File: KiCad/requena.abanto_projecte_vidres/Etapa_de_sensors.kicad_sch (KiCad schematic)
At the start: 0 parts

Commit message: avance sensores
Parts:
- added C1: 100nF, symbol Device:C
- added C2, C3: C, symbol Device:C
- added C4, C5, C6, C7, C8: 100nF, symbol Device:C_Small
- added R1, R2: R, symbol Device:R
- added U1: PN5120A0HN1, Package_DFN_QFN:HVQFN-32-1EP_5x5mm_P0.5mm_EP3.1x3.1mm, symbol RF_RFID:PN5120A0HN1
- added U2: MCP6001-OT, Package_TO_SOT_SMD:SOT-23-5, symbol Amplifier_Operational:MCP6001-OT
- added Y1: Crystal, symbol Device:Crystal
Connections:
- new net: C2.1, U1.21 (OSCIN), Y1.1
- new net: C3.1, U1.22 (OSCOUT), Y1.2
- new net: R1.2, R2.1, U2.4 (-)
- new net: C1.1, U1.16 (VMID)
- new net AN0: R2.2, U2.1
- new net GND: C1.2, C2.2, C3.2, C4.1, C5.1, C6.1, C7.1, C8.1, R1.1, U1.1 (A1), U1.10 (TVSS), U1.14 (TVSS), U1.18 (AVSS), U1.24 (ALE), U1.32 (A0), U1.33 (EP), U1.4 (DVSS), U1.5 (PVSS), U2.2 (V-)
- new net IRQ: U1.23 (IRQ)
- new net MISO: U1.17 (RX)
- new net MOSI: U1.11 (TX1)
- new net NRSTPD: U1.6 (~{NRSTPD})
- new net SCK: U1.13 (TX2)
- new net VCC: C4.2, C5.2, C6.2, C7.2, C8.2, U1.12 (TVDD), U1.15 (AVDD), U1.2 (PVDD), U1.3 (DVDD), U1.9 (SVDD), U2.5 (V+)
- new net V_SHUNT: U2.3 (+)
- no-connect marks 0 -> 7
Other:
- note added: "A INT0"
- note added: "A L'ANTENA"
- note added: "A RBXX"
- note added: "A RPXX"

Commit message: avance sensores
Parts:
- added SW1, SW3, SW4, SW5: SW_Omron_B3FS, symbol Switch:SW_Omron_B3FS
- added SW2: SW_Push_SPDT, symbol Switch:SW_Push_SPDT
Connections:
- net GND: now also SW1.1, SW3.1, SW4.1, SW5.1
- net VCC: now also SW2.2 (B)
- new net CLOSED_FC: SW2.3 (C)
- new net CLOSE_D: SW5.2
- new net DOWN_W: SW3.2
- new net OPEN_D: SW4.2
- new net OPEN_FC: SW2.1 (A)
- new net UP_W: SW1.2
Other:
- moved on the sheet: C1, C2, C3, C4, C5, C6, C7, C8, R1, R2, U1, U2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

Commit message: arreglos
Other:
- note removed: "A INT0"
- note removed: "A RPXX"
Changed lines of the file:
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@@
-		)
-	)
-	(text "A RPXX\n"
-		(exclude_from_sim no)
-		(at 94.234 148.59 0)
-		(effects
-			(font
-				(size 1.27 1.27)
-			)
 		)
 	)
@@
 		(effects
 			(font
-				(size 1.27 1.27)
-			)
-		)
-	)
-	(text "A RPXX\n"
-		(exclude_from_sim no)
-		(at 94.742 145.796 0)
-		(effects
-			(font
-				(size 1.27 1.27)
-			)
-		)
-	)
-	(text "A INT0\n"
-		(exclude_from_sim no)
-		(at 90.678 131.064 0)
-		(effects
-			(font
-				(size 1.27 1.27)
-			)
-		)
-	)
-	(text "A RPXX\n"
-		(exclude_from_sim no)
-		(at 22.352 133.604 0)
-		(effects
-			(font
-				(size 1.27 1.27)
-			)
-		)
-	)
-	(text "A RBXX\n"
-		(exclude_from_sim no)
-		(at 28.702 125.73 0)
-		(effects
-			(font

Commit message: clase
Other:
- note added: "A L'ANTENA =>>>Chip antena"
- note removed: "A L'ANTENA"
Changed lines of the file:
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@@
 		)
 	)
-	(text "A L'ANTENA\n"
+	(text "A L'ANTENA =>>>Chip antena\n"
 		(exclude_from_sim no)
 		(at 126.492 148.844 90)

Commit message: cambios de clase
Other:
- note removed: "A RBXX"
- moved on the sheet: R1, R2, SW1, SW2, SW3, SW4, SW5, U2

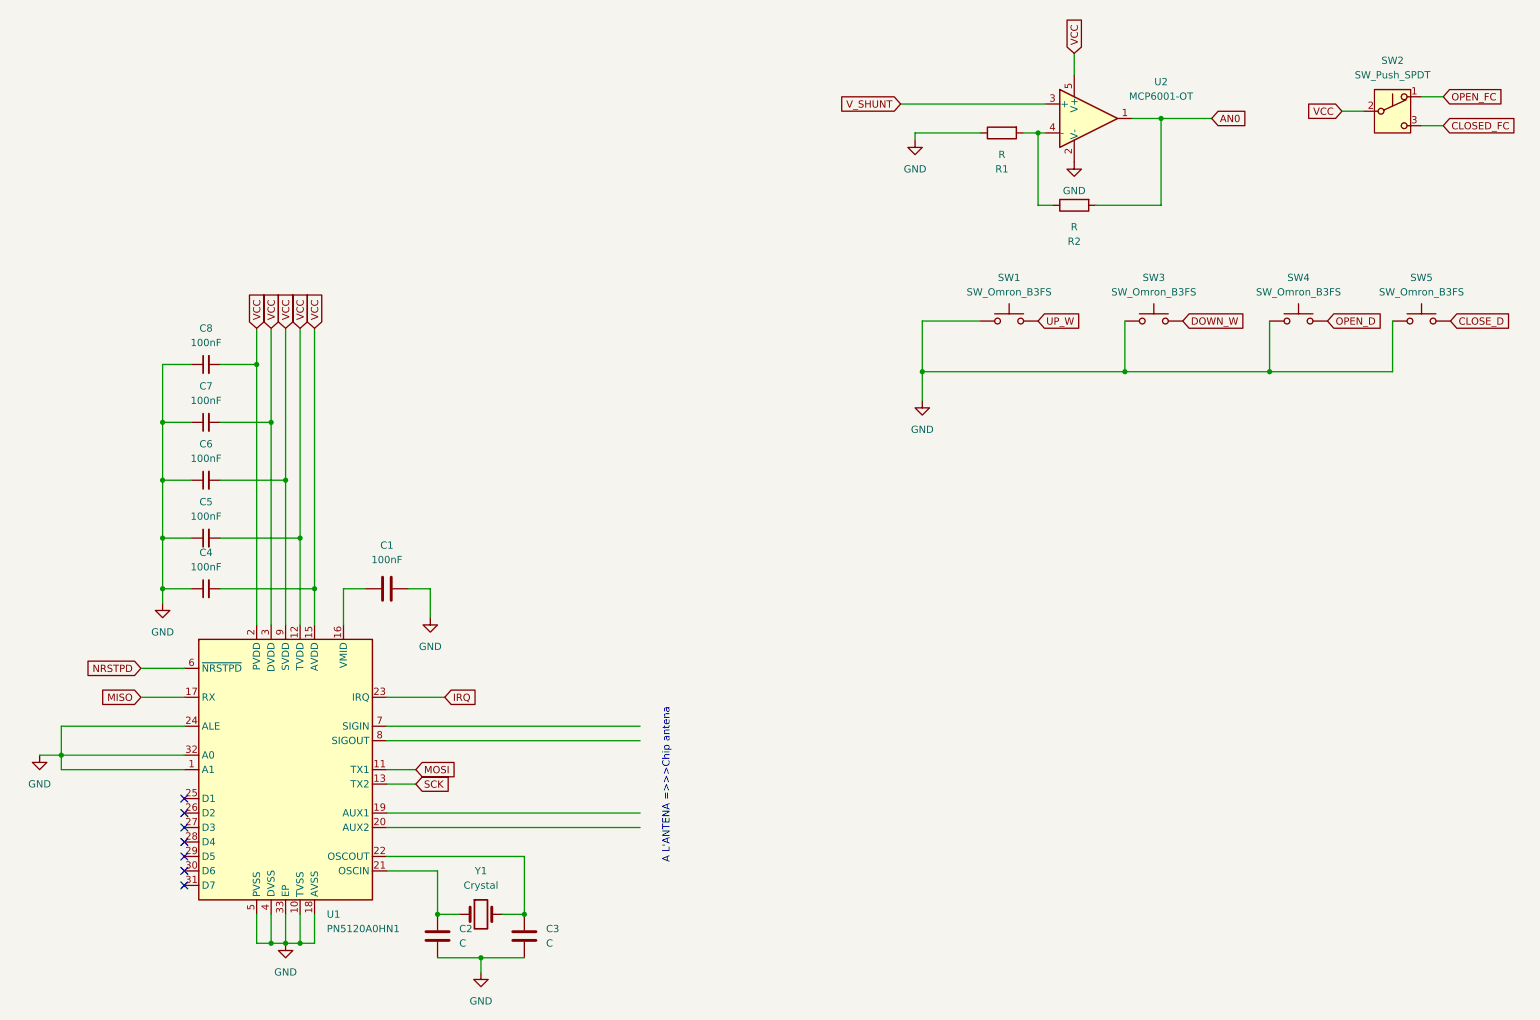
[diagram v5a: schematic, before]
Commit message: millora el esquematic
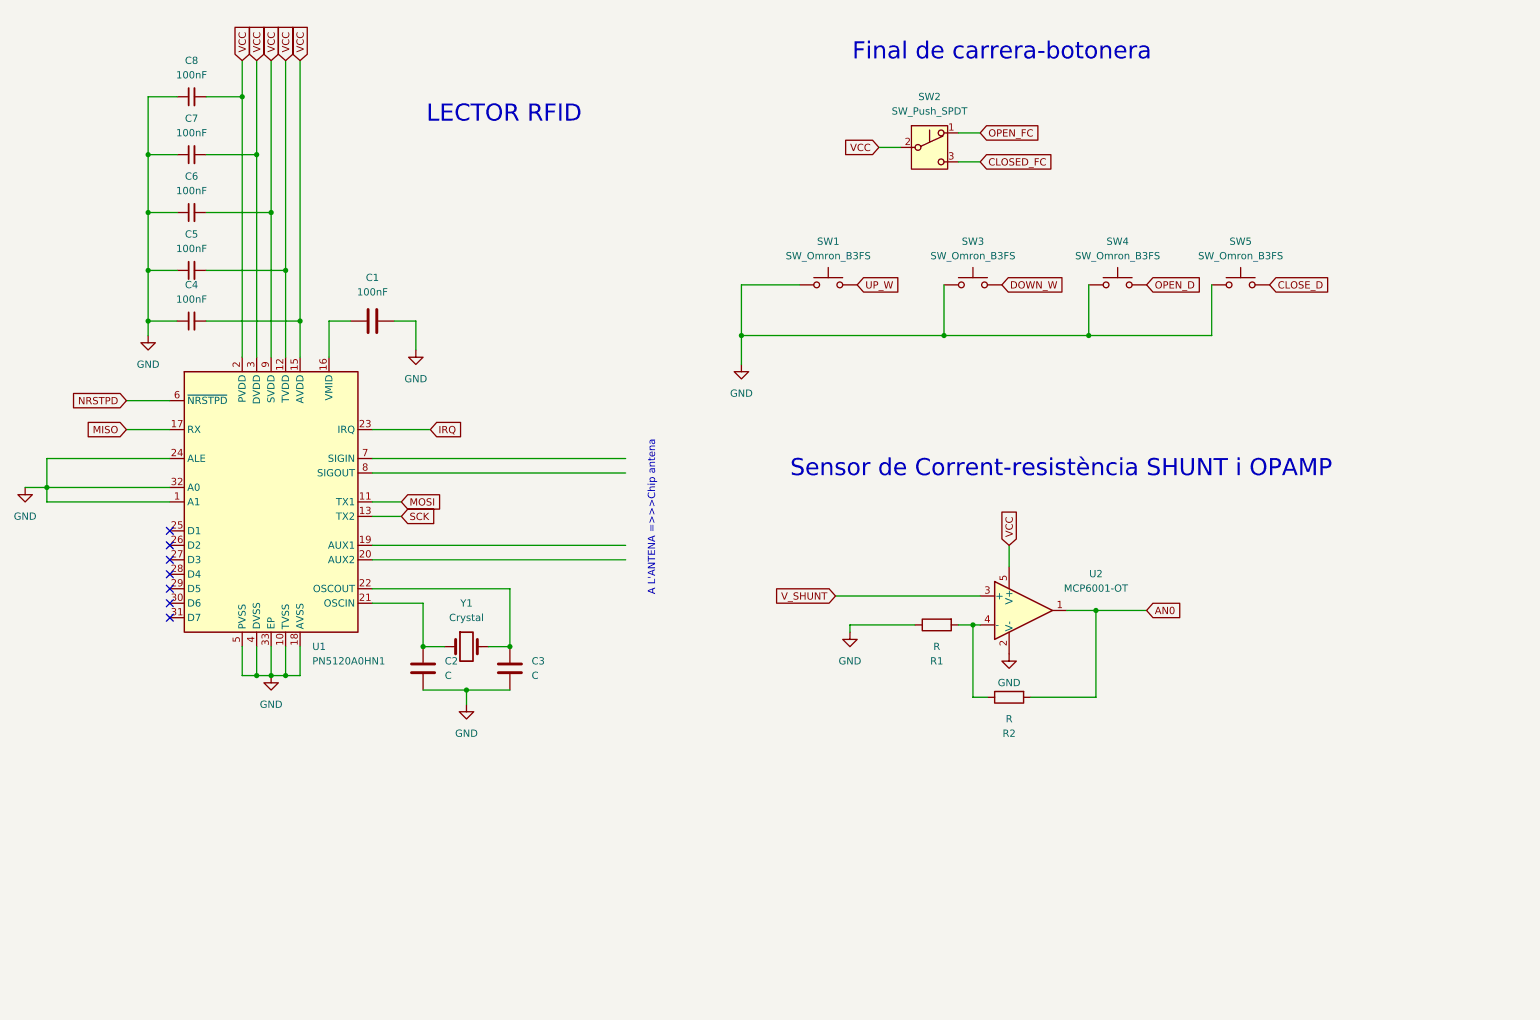
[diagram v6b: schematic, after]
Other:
- note added: "Final de carrera-botonera"
- note added: "LECTOR RFID"
- note added: "Sensor de Corrent-resistència SHUNT i OPAMP"
- moved on the sheet: C1, C2, C3, C4, C5, C6, C7, C8, R1, R2, SW1, SW2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

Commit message: Millora projecte 1
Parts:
- removed R1, R2: R, symbol Device:R
- removed U2: MCP6001-OT, Package_TO_SOT_SMD:SOT-23-5, symbol Amplifier_Operational:MCP6001-OT

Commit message: millora
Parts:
- removed C1: 100nF, symbol Device:C
- removed C2, C3: C, symbol Device:C
- removed C4, C5, C6, C7, C8: 100nF, symbol Device:C_Small
- removed SW1, SW3, SW4, SW5: SW_Omron_B3FS, symbol Switch:SW_Omron_B3FS
- removed SW2: SW_Push_SPDT, symbol Switch:SW_Push_SPDT
- removed U1: PN5120A0HN1, Package_DFN_QFN:HVQFN-32-1EP_5x5mm_P0.5mm_EP3.1x3.1mm, symbol RF_RFID:PN5120A0HN1
- removed Y1: Crystal, symbol Device:Crystal
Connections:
- no-connect marks 7 -> 0
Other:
- note removed: "A L'ANTENA =>>>Chip antena"
- note removed: "Final de carrera-botonera"
- note removed: "LECTOR RFID"
- note removed: "Sensor de Corrent-resistència SHUNT i OPAMP"
